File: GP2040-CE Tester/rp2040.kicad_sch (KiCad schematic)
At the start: 0 parts

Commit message: adding most of the components, and schematic connections
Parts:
- added C1, C10, C2, C3, C4, C5, C6, C7, C9: 100nF, Capacitor_SMD:C_0603_1608Metric, symbol Device:C
- added C11, C8: 1uF, Capacitor_SMD:C_0603_1608Metric, symbol Device:C
- added C12: 100n, Capacitor_SMD:C_0603_1608Metric, symbol Device:C
- added R1, R2: 24.7, Resistor_SMD:R_0603_1608Metric, symbol Device:R
- added R4: 1k, Resistor_SMD:R_0603_1608Metric, symbol Device:R
- added U1: RP2040, Package_DFN_QFN:QFN-56-1EP_7x7mm_P0.4mm_EP3.2x3.2mm, symbol MCU_RaspberryPi:RP2040
- added U2: SIT2018BE-S8-33N-12.000000G, GP2040-CE-Tester:SiT1630-S, symbol GP2040-CE-Tester:SIT2018BE-S8-33N-12.000000G
- added U3: W25Q128JVS, Package_SO:SOIC-8_5.23x5.23mm_P1.27mm, symbol Memory_Flash:W25Q128JVS
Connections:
- new net: R1.1, U1.47 (USB_DP)
- new net: R2.2, U1.46 (USB_DM)
- new net +1V1: C10.1, C11.1, C9.1, U1.23 (DVDD), U1.45 (VREG_VOUT), U1.50 (DVDD)
- new net +3.3V: C1.1, C12.1, C2.1, C3.1, C4.1, C5.1, C6.1, C7.1, C8.1, U1.1 (IOVDD), U1.10 (IOVDD), U1.22 (IOVDD), U1.33 (IOVDD), U1.42 (IOVDD), U1.43 (ADC_AVDD), U1.44 (VREG_IN), U1.48 (USB_VDD), U1.49 (IOVDD), U2.4 (VDD), U3.8 (VCC)
- new net GND: C1.2, C10.2, C11.2, C12.2, C2.2, C3.2, C4.2, C5.2, C6.2, C7.2, C8.2, C9.2, U1.19 (TESTEN), U1.57 (GND), U2.1 (GND), U3.4 (GND)
- new net GPIO0: U1.2 (GPIO0)
- new net GPIO1: U1.3 (GPIO1)
- new net GPIO10: U1.13 (GPIO10)
- new net GPIO11: U1.14 (GPIO11)
- new net GPIO12: U1.15 (GPIO12)
- new net GPIO13: U1.16 (GPIO13)
- new net GPIO14: U1.17 (GPIO14)
- new net GPIO15: U1.18 (GPIO15)
- new net GPIO16: U1.27 (GPIO16)
- new net GPIO17: U1.28 (GPIO17)
- new net GPIO18: U1.29 (GPIO18)
- new net GPIO19: U1.30 (GPIO19)
- new net GPIO2: U1.4 (GPIO2)
- new net GPIO20: U1.31 (GPIO20)
- new net GPIO21: U1.32 (GPIO21)
- new net GPIO22: U1.34 (GPIO22)
- new net GPIO23: U1.35 (GPIO23)
- new net GPIO24: U1.36 (GPIO24)
- new net GPIO25: U1.37 (GPIO25)
- new net GPIO26_ADC0: U1.38 (GPIO26_ADC0)
- new net GPIO27_ADC1: U1.39 (GPIO27_ADC1)
- new net GPIO28_ADC2: U1.40 (GPIO28_ADC2)
- new net GPIO29_ADC3: U1.41 (GPIO29_ADC3)
- new net GPIO3: U1.5 (GPIO3)
- new net GPIO4: U1.6 (GPIO4)
- new net GPIO5: U1.7 (GPIO5)
- new net GPIO6: U1.8 (GPIO6)
- new net GPIO7: U1.9 (GPIO7)
- new net GPIO8: U1.11 (GPIO8)
- new net GPIO9: U1.12 (GPIO9)
- new net QSPI_SCLK: U1.52 (QSPI_SCLK), U3.6 (CLK)
- new net QSPI_SD0: U1.53 (QSPI_SD0), U3.5 (DI(IO0))
- new net QSPI_SD1: U1.55 (QSPI_SD1), U3.2 (DO(IO1))
- new net QSPI_SD2: U1.54 (QSPI_SD2), U3.3 (IO2)
- new net QSPI_SD3: U1.51 (QSPI_SD3), U3.7 (IO3)
- new net QSPI_SS: R4.2, U1.56 (QSPI_SS), U3.1 (~{CS})
- new net RP2040D+: R1.2
- new net RP2040D-: R2.1
- new net RUN: U1.26 (RUN)
- new net SWCLK: U1.24 (SWCLK)
- new net SWD: U1.25 (SWD)
- new net clock: U1.20 (XIN), U2.5 (OUT)
- new net ~{USB_BOOT}: R4.1
- no-connect marks 0 -> 2

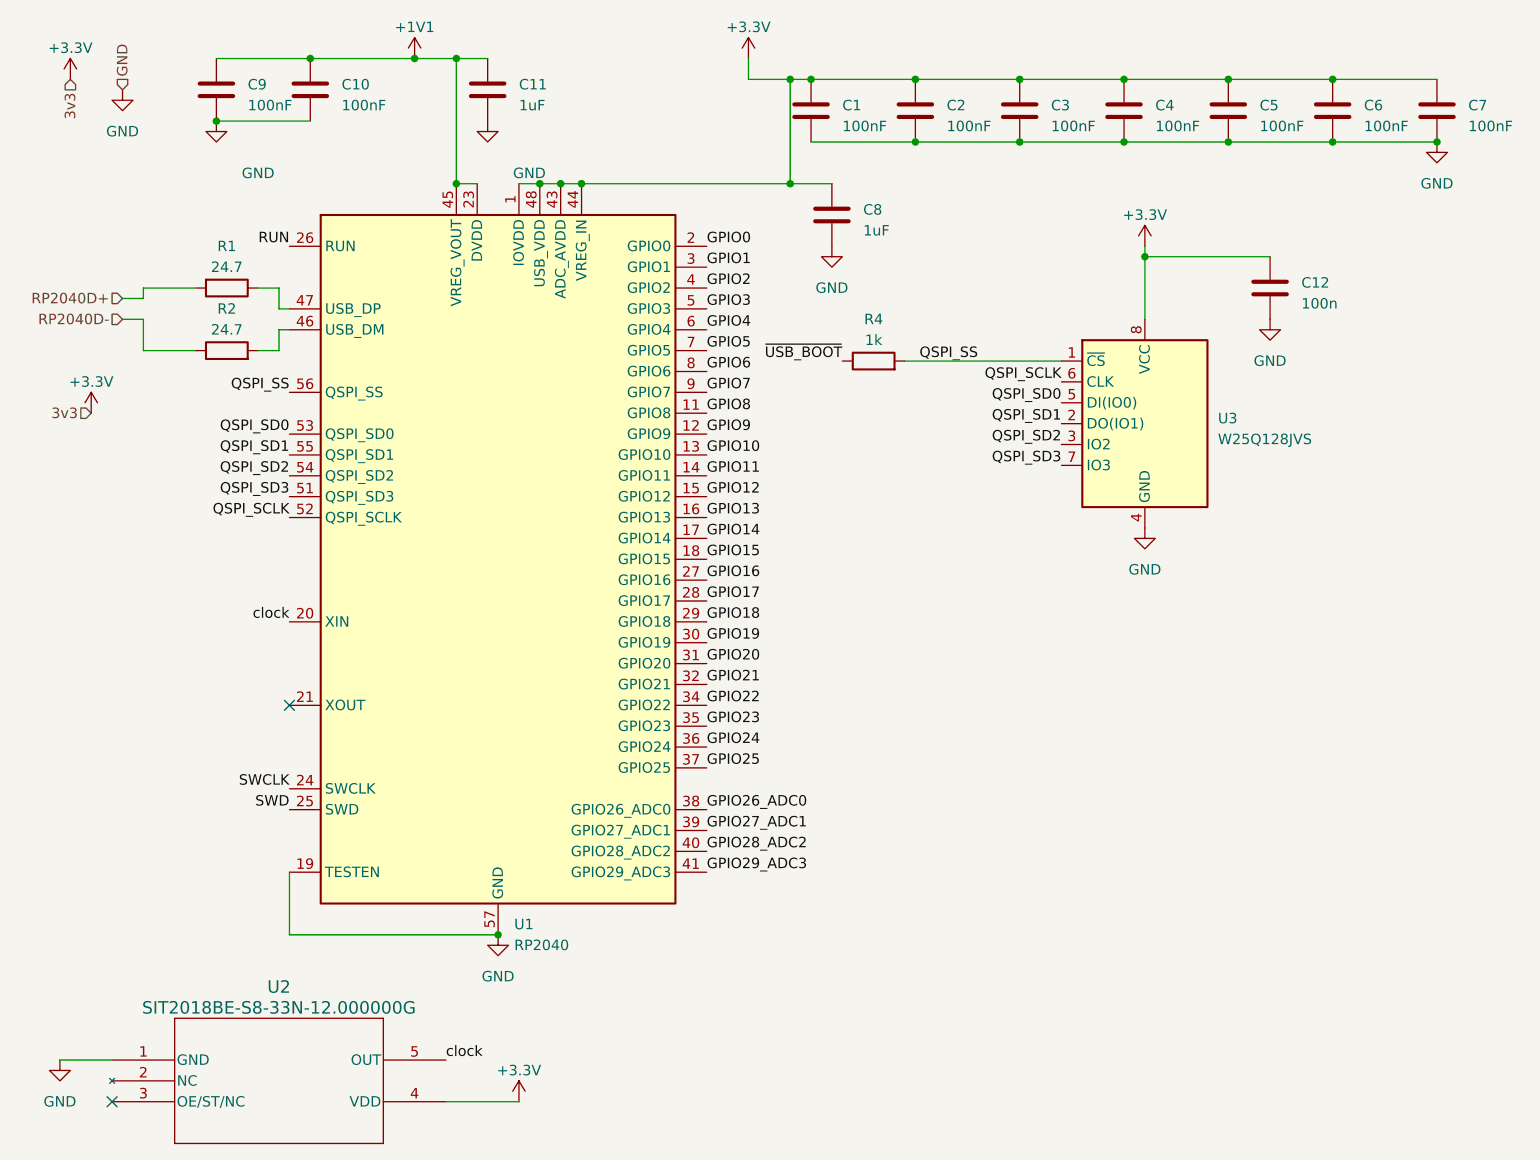
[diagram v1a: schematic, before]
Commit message: adding most of the components, and schematic connections
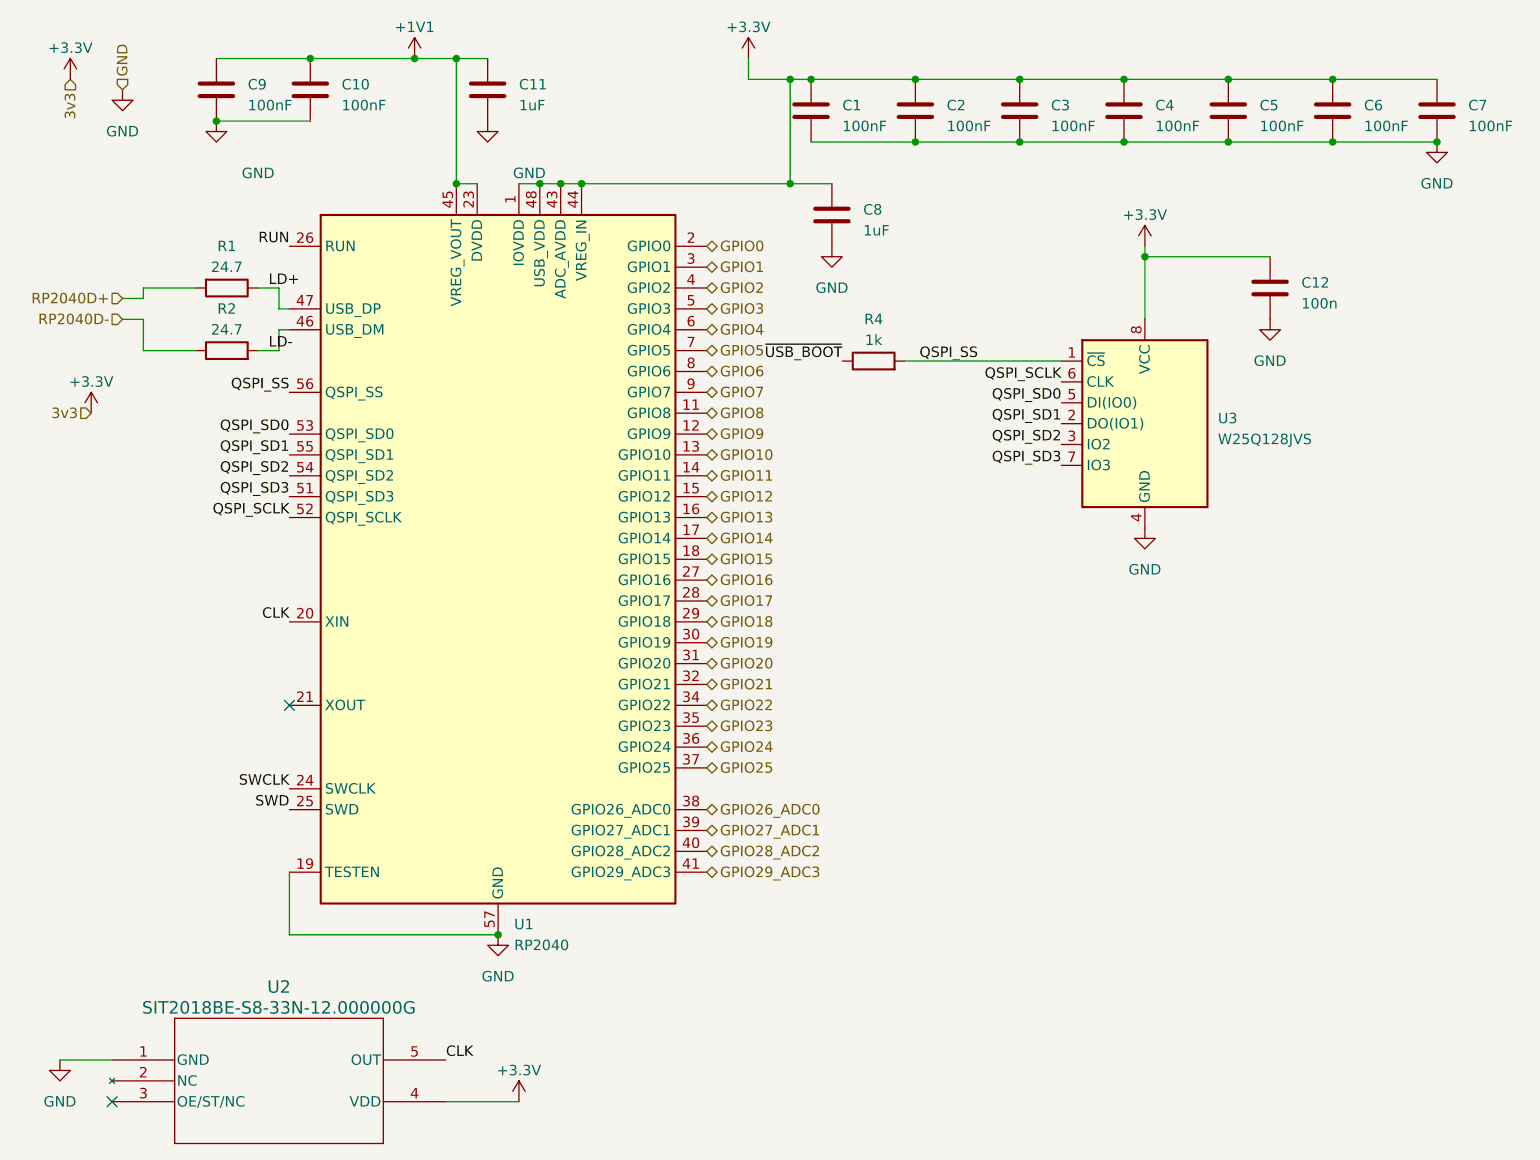
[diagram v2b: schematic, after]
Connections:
- net LD+: now reaches R1.1, U1.47 (USB_DP)
- net LD-: now reaches R2.2, U1.46 (USB_DM)
- net clock renamed CLK
